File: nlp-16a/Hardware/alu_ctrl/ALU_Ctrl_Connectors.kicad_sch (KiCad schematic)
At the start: 83 parts, among them J1 Screw_Terminal_01x02, J10 Conn_02x08_Odd_Even, J2 Conn_02x20_Odd_Even, J3 Conn_02x10_Counter_Clockwise, J4 Conn_02x10_Counter_Clockwise, J5 Conn_02x10_Counter_Clockwise, J6 Conn_02x10_Counter_Clockwise, J7 Conn_02x10_Counter_Clockwise, J8 Conn_02x08_Odd_Even, J9 Conn_02x08_Odd_Even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

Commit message: 基板の途中経過
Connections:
- net Y_Flag_sel: now also J5.4 (Pin_4); no longer J5.2 (Pin_2)
- net carry_flag: now also J5.2 (Pin_2); no longer J5.4 (Pin_4)
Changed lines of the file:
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@@
     )
   )
-  (global_label "carry_flag" (shape output) (at 218.44 96.52 180) (fields_autoplaced)
+  (global_label "carry_flag" (shape output) (at 218.44 99.06 180) (fields_autoplaced)
     (effects (font (size 1.27 1.27)) (justify right))
-    (property "Intersheet References" "${INTERSHEET_REFS}" (id 0) (at 206.5926 96.4406 0)
+    (property "Intersheet References" "${INTERSHEET_REFS}" (id 0) (at 206.5926 98.9806 0)
       (effects (font (size 1.27 1.27)) (justify right) hide)
     )
@@
     )
   )
-  (global_label "Y_Flag_sel" (shape output) (at 218.44 99.06 180) (fields_autoplaced)
+  (global_label "Y_Flag_sel" (shape output) (at 218.44 96.52 180) (fields_autoplaced)
     (effects (font (size 1.27 1.27)) (justify right))
-    (property "Intersheet References" "${INTERSHEET_REFS}" (id 0) (at 206.1693 98.9806 0)
+    (property "Intersheet References" "${INTERSHEET_REFS}" (id 0) (at 206.1693 96.4406 0)
       (effects (font (size 1.27 1.27)) (justify right) hide)
     )

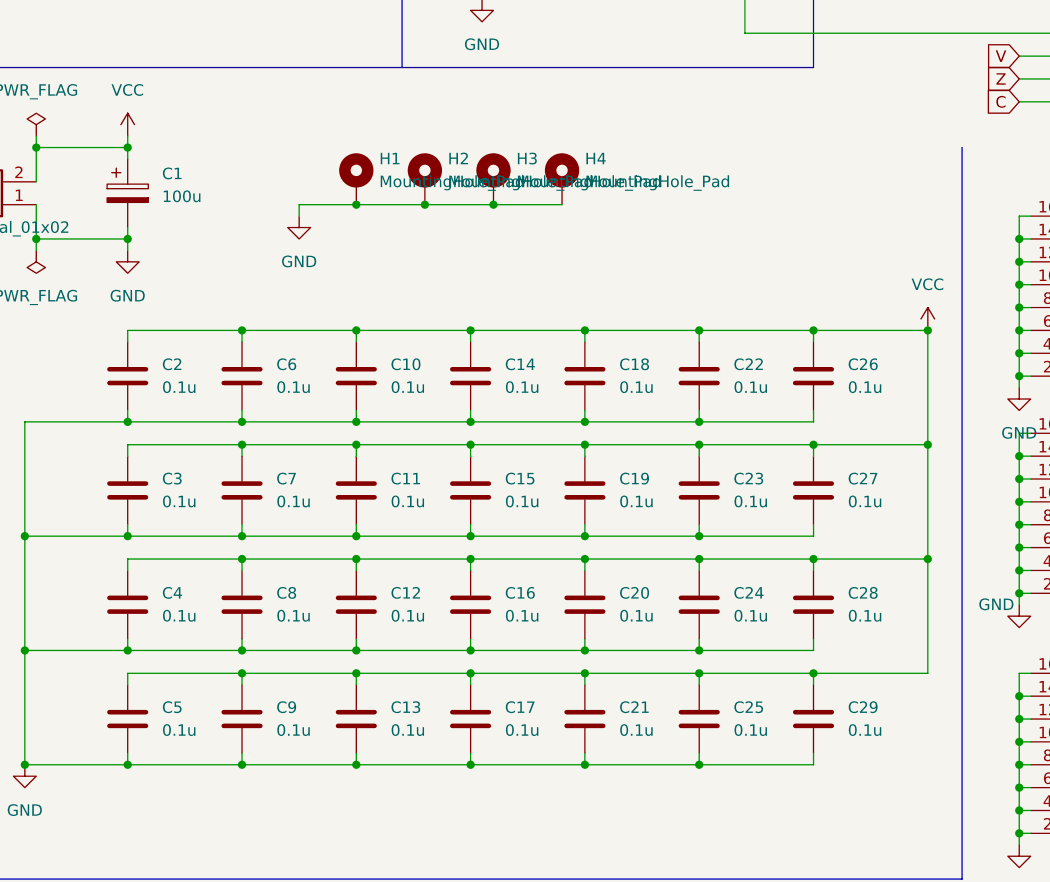
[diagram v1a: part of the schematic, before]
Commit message: githubのページから作業が見られるように思いつきで基板，回路のプレビューを追加．以下ではなるべく変更時にプレビューを更新
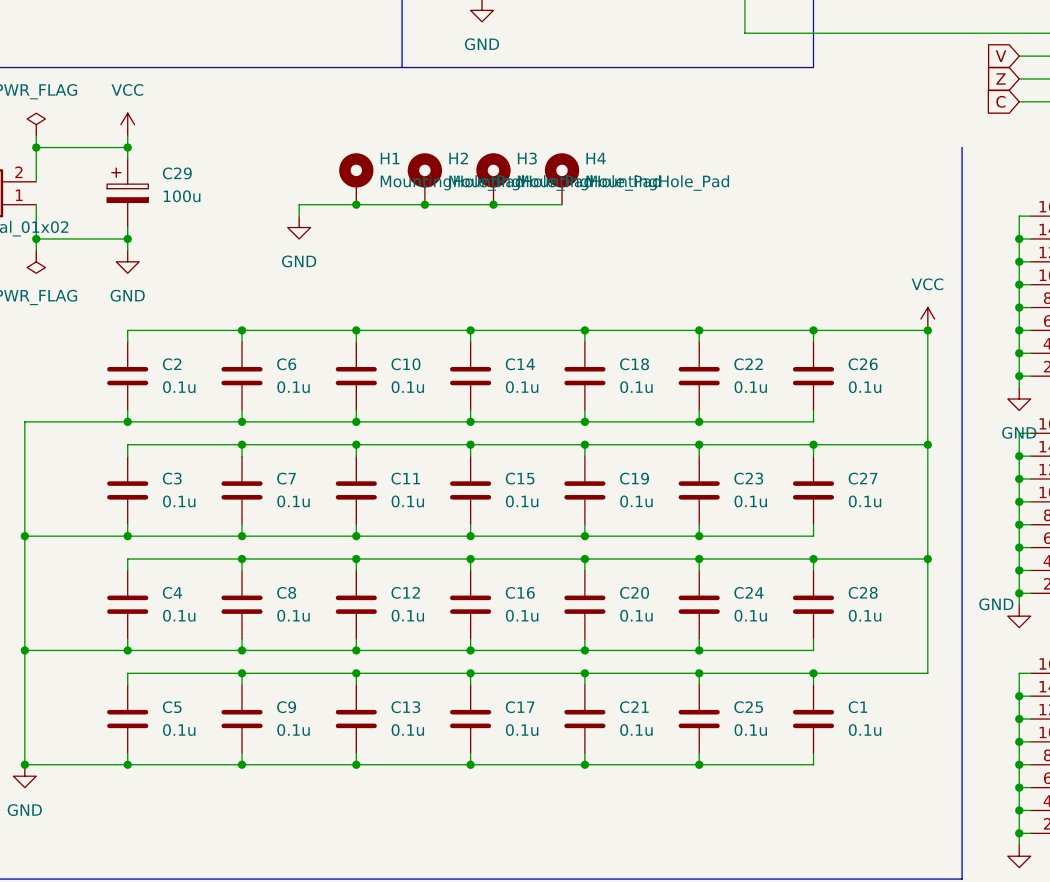
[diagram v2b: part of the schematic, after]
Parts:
- renumbered C29 to C1, C1 to C29
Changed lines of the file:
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@@
   (symbol (lib_id "Device:C_Polarized") (at 48.26 115.57 0) (unit 1)
     (in_bom yes) (on_board yes) (fields_autoplaced)
-    (property "Reference" "C1" (id 0) (at 52.07 113.4109 0)
+    (property "Reference" "C29" (id 0) (at 52.07 113.4109 0)
       (effects (font (size 1.27 1.27)) (justify left))
     )
@@
   (symbol (lib_id "Device:C") (at 124.46 173.99 180) (unit 1)
     (in_bom yes) (on_board yes) (fields_autoplaced)
-    (property "Reference" "C29" (id 0) (at 128.27 172.7199 0)
+    (property "Reference" "C1" (id 0) (at 128.27 172.7199 0)
       (effects (font (size 1.27 1.27)) (justify right))
     )

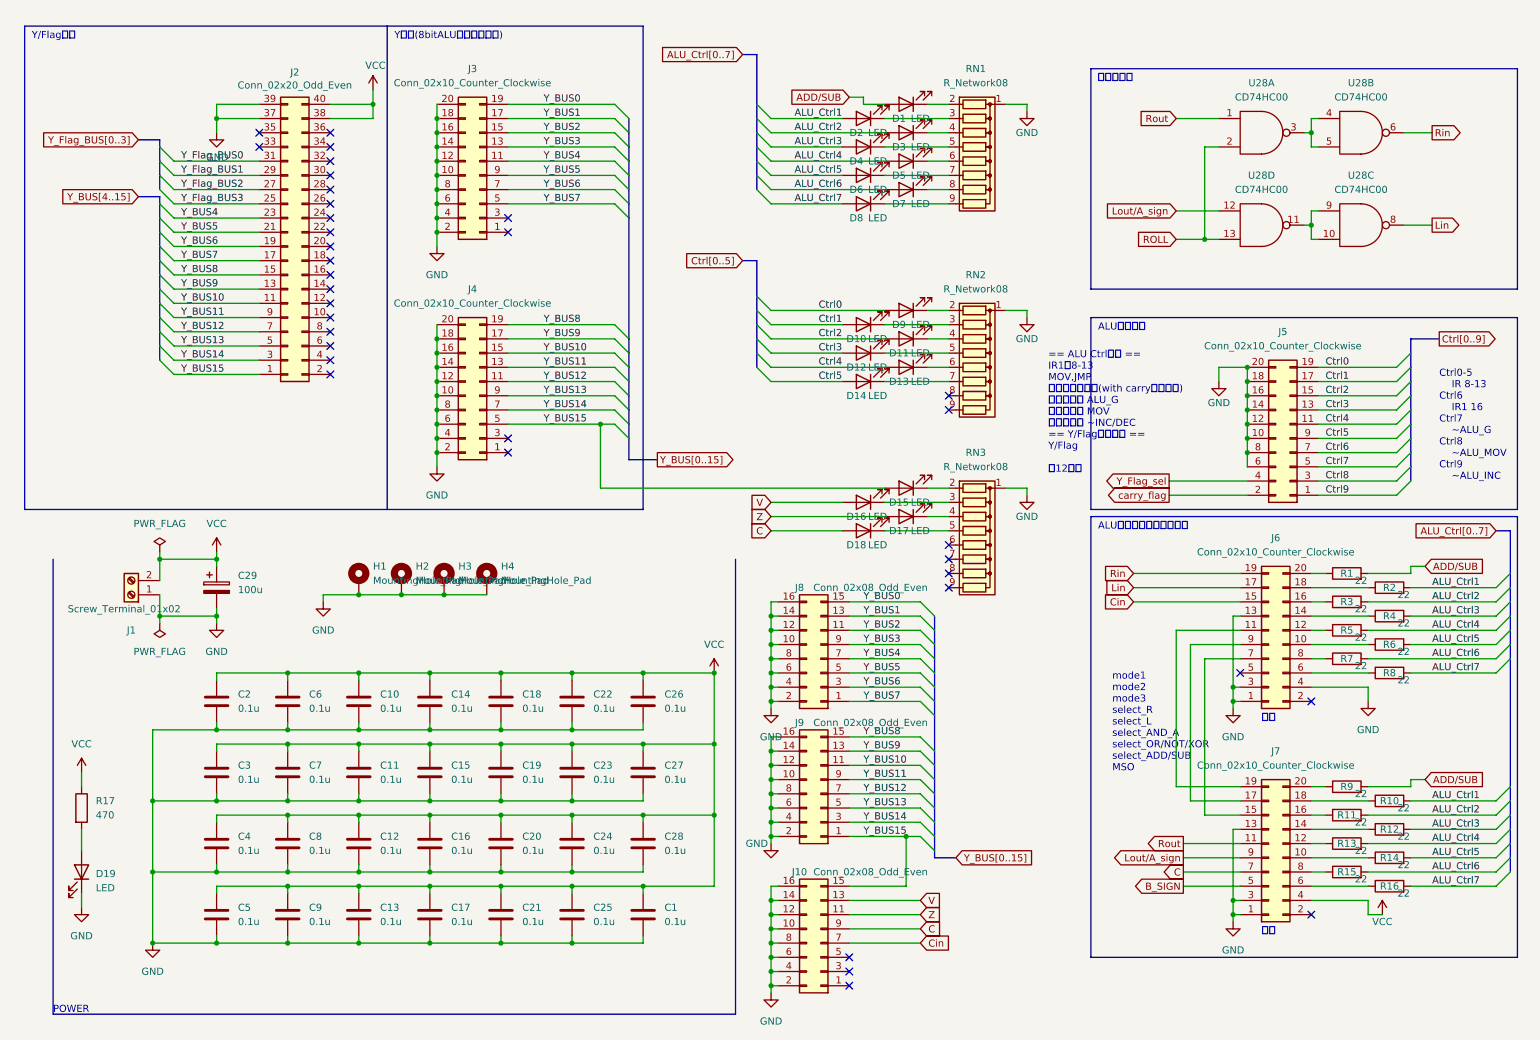
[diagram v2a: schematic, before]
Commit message: 電源バス，シルクスクリーン更新
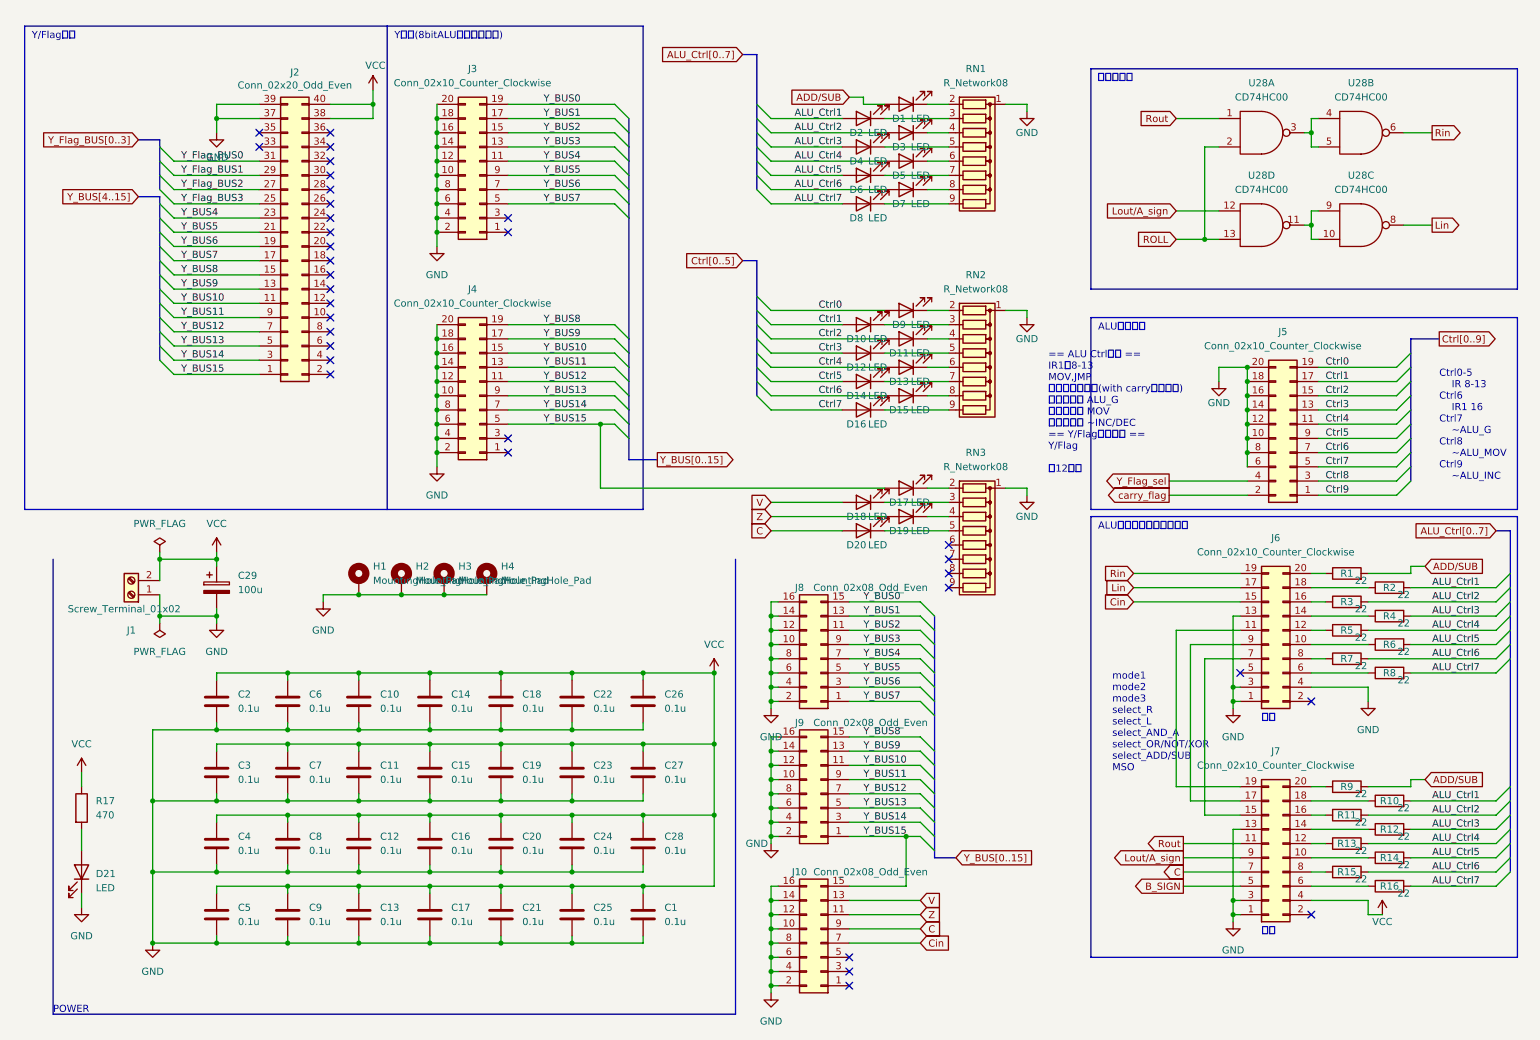
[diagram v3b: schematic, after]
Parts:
- added D15, D16: LED, LED_THT:LED_D3.0mm, symbol Device:LED
- renumbered D15 to D17, D16 to D18, D17 to D19, D18 to D20, D19 to D21
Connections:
- net Ctrl6: now also D15.2 (A)
- net Ctrl7: now also D16.2 (A)
- net at RN2.8 (R7): now also D15.1 (K)
- net at RN2.9 (R8): now also D16.1 (K)
- no-connect marks 36 -> 34
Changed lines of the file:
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@@
   (no_connect (at 179.07 115.57))
   (no_connect (at 179.07 113.03))
-  (no_connect (at 179.07 81.28))
-  (no_connect (at 179.07 83.82))
   (no_connect (at 68.58 54.61))
   (no_connect (at 68.58 67.31))
@@
     (stroke (width 0) (type default) (color 0 0 0 0))
   )
+  (bus_entry (at 144.78 81.28) (size 2.54 2.54)
+    (stroke (width 0) (type default) (color 0 0 0 0))
+  )
   (bus_entry (at 259.08 86.36) (size 2.54 -2.54)
     (stroke (width 0) (type default) (color 0 0 0 0))
@@
     (stroke (width 0) (type default) (color 0 0 0 0))
   )
+  (bus_entry (at 144.78 78.74) (size 2.54 2.54)
+    (stroke (width 0) (type default) (color 0 0 0 0))
+  )
   (bus_entry (at 119.38 71.12) (size 2.54 2.54)
     (stroke (width 0) (type default) (color 0 0 0 0))
@@
     (stroke (width 0) (type default) (color 0 0 0 0))
   )
+  (wire (pts (xy 147.32 83.82) (xy 160.02 83.82))
+    (stroke (width 0) (type default) (color 0 0 0 0))
+  )
   (wire (pts (xy 99.06 140.97) (xy 111.76 140.97))
     (stroke (width 0) (type default) (color 0 0 0 0))
@@
     (stroke (width 0) (type default) (color 0 0 0 0))
   )
+  (wire (pts (xy 147.32 81.28) (xy 167.64 81.28))
+    (stroke (width 0) (type default) (color 0 0 0 0))
+  )
   (wire (pts (xy 147.32 120.65) (xy 148.59 120.65))
     (stroke (width 0) (type default) (color 0 0 0 0))
@@
     (stroke (width 0) (type default) (color 0 0 0 0))
   )
+  (bus (pts (xy 144.78 76.2) (xy 144.78 78.74))
+    (stroke (width 0) (type default) (color 0 0 0 0))
+  )
   (wire (pts (xy 124.46 165.1) (xy 124.46 166.37))
     (stroke (width 0) (type default) (color 0 0 0 0))
@@
     (stroke (width 0) (type default) (color 0 0 0 0))
   )
+  (wire (pts (xy 175.26 81.28) (xy 179.07 81.28))
+    (stroke (width 0) (type default) (color 0 0 0 0))
+  )
   (wire (pts (xy 87.63 91.44) (xy 87.63 88.9))
     (stroke (width 0) (type default) (color 0 0 0 0))
@@
     (stroke (width 0) (type default) (color 0 0 0 0))
   )
+  (wire (pts (xy 167.64 83.82) (xy 179.07 83.82))
+    (stroke (width 0) (type default) (color 0 0 0 0))
+  )
   (bus (pts (xy 279.4 128.27) (xy 279.4 151.13))
     (stroke (width 0) (type default) (color 0 0 0 0))
@@
     (stroke (width 0) (type default) (color 0 0 0 0))
   )
+  (bus (pts (xy 144.78 78.74) (xy 144.78 81.28))
+    (stroke (width 0) (type default) (color 0 0 0 0))
+  )
   (bus (pts (xy 176.53 149.86) (xy 176.53 152.4))
     (stroke (width 0) (type default) (color 0 0 0 0))
@@
     (effects (font (size 1.27 1.27)) (justify left bottom))
   )
+  (label "Ctrl6" (at 160.02 81.28 180)
+    (effects (font (size 1.27 1.27)) (justify right bottom))
+  )
   (label "ALU_Ctrl1" (at 265.43 115.57 0)
     (effects (font (size 1.27 1.27)) (justify left bottom))
@@
     (effects (font (size 1.27 1.27)) (justify left bottom))
   )
+  (label "Ctrl7" (at 160.02 83.82 180)
+    (effects (font (size 1.27 1.27)) (justify right bottom))
+  )
   (label "Y_BUS14" (at 106.68 83.82 0)
     (effects (font (size 1.27 1.27)) (justify left bottom))
@@
   (symbol (lib_id "Device:LED") (at 171.45 97.79 180) (unit 1)
     (in_bom yes) (on_board yes)
-    (property "Reference" "D15" (id 0) (at 170.18 100.33 0))
+    (property "Reference" "D17" (id 0) (at 170.18 100.33 0))
     (property "Value" "LED" (id 1) (at 173.99 100.33 0))
     (property "Footprint" "LED_THT:LED_D3.0mm" (id 2) (at 171.45 97.79 0)
@@
   (symbol (lib_id "Device:LED") (at 171.45 102.87 180) (unit 1)
     (in_bom yes) (on_board yes)
-    (property "Reference" "D17" (id 0) (at 170.18 105.41 0))
+    (property "Reference" "D19" (id 0) (at 170.18 105.41 0))
     (property "Value" "LED" (id 1) (at 173.99 105.41 0))
     (property "Footprint" "LED_THT:LED_D3.0mm" (id 2) (at 171.45 102.87 0)
@@
     (pin "1")
   )
+  (symbol (lib_id "Device:LED") (at 171.45 81.28 180) (unit 1)
+    (in_bom yes) (on_board yes)
+    (property "Reference" "D15" (id 0) (at 170.18 83.82 0))
+    (property "Value" "LED" (id 1) (at 173.99 83.82 0))
+    (property "Footprint" "LED_THT:LED_D3.0mm" (id 2) (at 171.45 81.28 0)
+      (effects (font (size 1.27 1.27)) hide)
+    )
+    (property "Datasheet" "~" (id 3) (at 171.45 81.28 0)
+      (effects (font (size 1.27 1.27)) hide)
+    )
+    (pin "1")
+    (pin "2")
+  )
   (symbol (lib_id "power:VCC") (at 48.26 109.22 0) (unit 1)
     (in_bom yes) (on_board yes) (fields_autoplaced)
@@
   (symbol (lib_id "Device:LED") (at 163.83 100.33 180) (unit 1)
     (in_bom yes) (on_board yes)
-    (property "Reference" "D16" (id 0) (at 162.56 102.87 0))
+    (property "Reference" "D18" (id 0) (at 162.56 102.87 0))
     (property "Value" "LED" (id 1) (at 166.37 102.87 0))
     (property "Footprint" "LED_THT:LED_D3.0mm" (id 2) (at 163.83 100.33 0)
@@
   (symbol (lib_id "Device:LED") (at 24.13 166.37 270) (mirror x) (unit 1)
     (in_bom yes) (on_board yes) (fields_autoplaced)
-    (property "Reference" "D19" (id 0) (at 26.67 166.6874 90)
+    (property "Reference" "D21" (id 0) (at 26.67 166.6874 90)
       (effects (font (size 1.27 1.27)) (justify left))
     )
@@
   (symbol (lib_id "Device:LED") (at 163.83 105.41 180) (unit 1)
     (in_bom yes) (on_board yes)
-    (property "Reference" "D18" (id 0) (at 162.56 107.95 0))
+    (property "Reference" "D20" (id 0) (at 162.56 107.95 0))
     (property "Value" "LED" (id 1) (at 166.37 107.95 0))
     (property "Footprint" "LED_THT:LED_D3.0mm" (id 2) (at 163.83 105.41 0)
@@
       (effects (font (size 1.27 1.27)) hide)
     )
+    (pin "1")
+    (pin "2")
+  )
+  (symbol (lib_id "Device:LED") (at 163.83 83.82 180) (unit 1)
+    (in_bom yes) (on_board yes)
+    (property "Reference" "D16" (id 0) (at 162.56 86.36 0))
+    (property "Value" "LED" (id 1) (at 166.37 86.36 0))
+    (property "Footprint" "LED_THT:LED_D3.0mm" (id 2) (at 163.83 83.82 0)
+      (effects (font (size 1.27 1.27)) hide)
+    )
+    (property "Datasheet" "~" (id 3) (at 163.83 83.82 0)
+      (effects (font (size 1.27 1.27)) hide)
+    )
